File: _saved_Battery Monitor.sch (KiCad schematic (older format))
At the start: 90 parts, among them J11 Conn_01x07, J12 Conn_01x12, Q10 Q_NMOS_DGS, Q11 Q_NMOS_DGS, Q12 Q_NMOS_DGS, Q13 Q_NMOS_DGS, Q14 Q_NMOS_DGS, Q15 Q_NMOS_DGS, Q16 Q_NMOS_DGS, Q6 Q_NMOS_DGS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

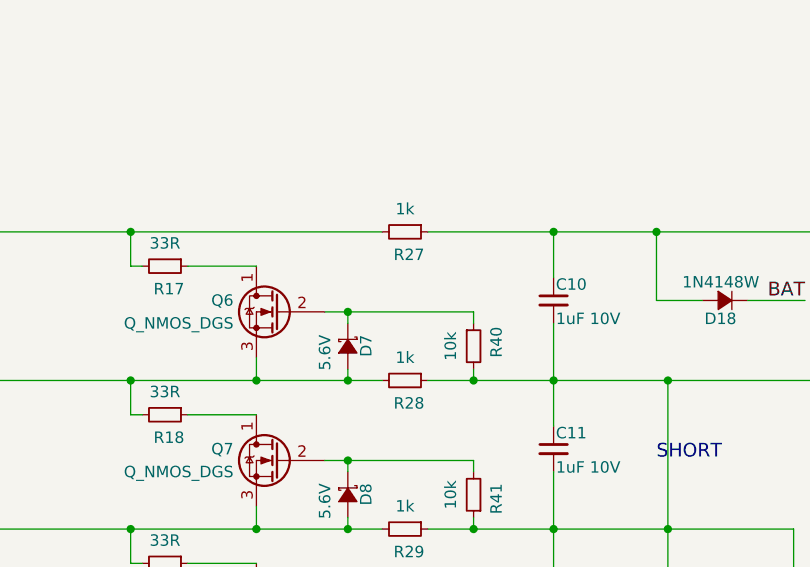
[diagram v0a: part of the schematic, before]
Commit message: Updated top-level connections and added MCU
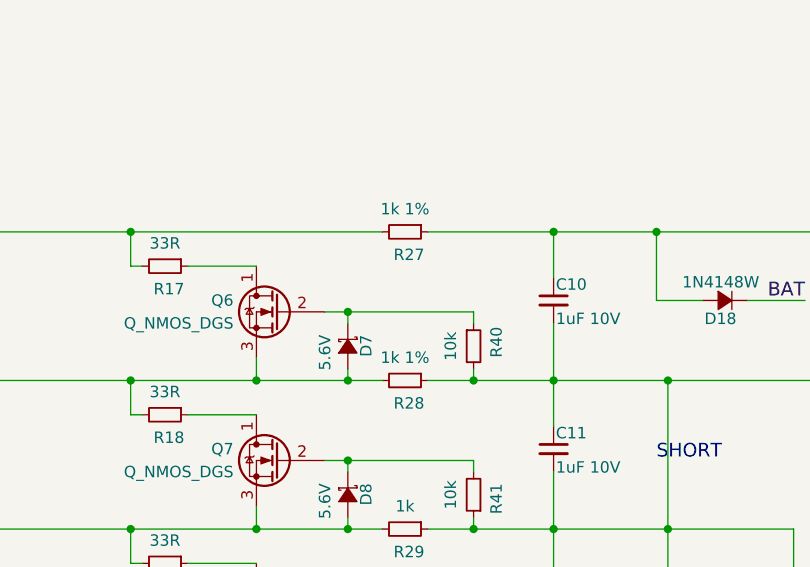
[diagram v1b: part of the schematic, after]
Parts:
- R27, R28: value 1k -> 1k 1%
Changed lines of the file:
@@
 P 2900 750
 F 0 "R27" V 3000 700 50  0000 L CNN
-F 1 "1k" V 2800 750 50  0000 C CNN
+F 1 "1k 1%" V 2800 750 50  0000 C CNN
 F 2 "Resistor_SMD:R_0603_1608Metric" H 2900 750 50  0001 C CNN
 F 3 "" H 2900 750 50  0001 C CNN
@@
 P 2900 1400
 F 0 "R28" V 3000 1350 50  0000 L CNN
-F 1 "1k" V 2800 1400 50  0000 C CNN
+F 1 "1k 1%" V 2800 1400 50  0000 C CNN
 F 2 "Resistor_SMD:R_0603_1608Metric" H 2900 1400 50  0001 C CNN
 F 3 "" H 2900 1400 50  0001 C CNN
